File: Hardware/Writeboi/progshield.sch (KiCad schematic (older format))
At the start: 14 parts, among them J1 GB-CART, J2 AUX_POW, SW1 SW_Push, U1 SST39SF040

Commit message: Update capacitor value
Set decoupling capacitor value to 100n
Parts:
- C1: value C -> 100n
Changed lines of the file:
@@
 P 8100 1500
 F 0 "C1" V 7848 1500 50  0000 C CNN
-F 1 "C" V 7939 1500 50  0000 C CNN
+F 1 "100n" V 7939 1500 50  0000 C CNN
 F 2 "Capacitor_THT:CP_Radial_D5.0mm_P2.50mm" H 8138 1350 50  0001 C CNN
 F 3 "~" H 8100 1500 50  0001 C CNN

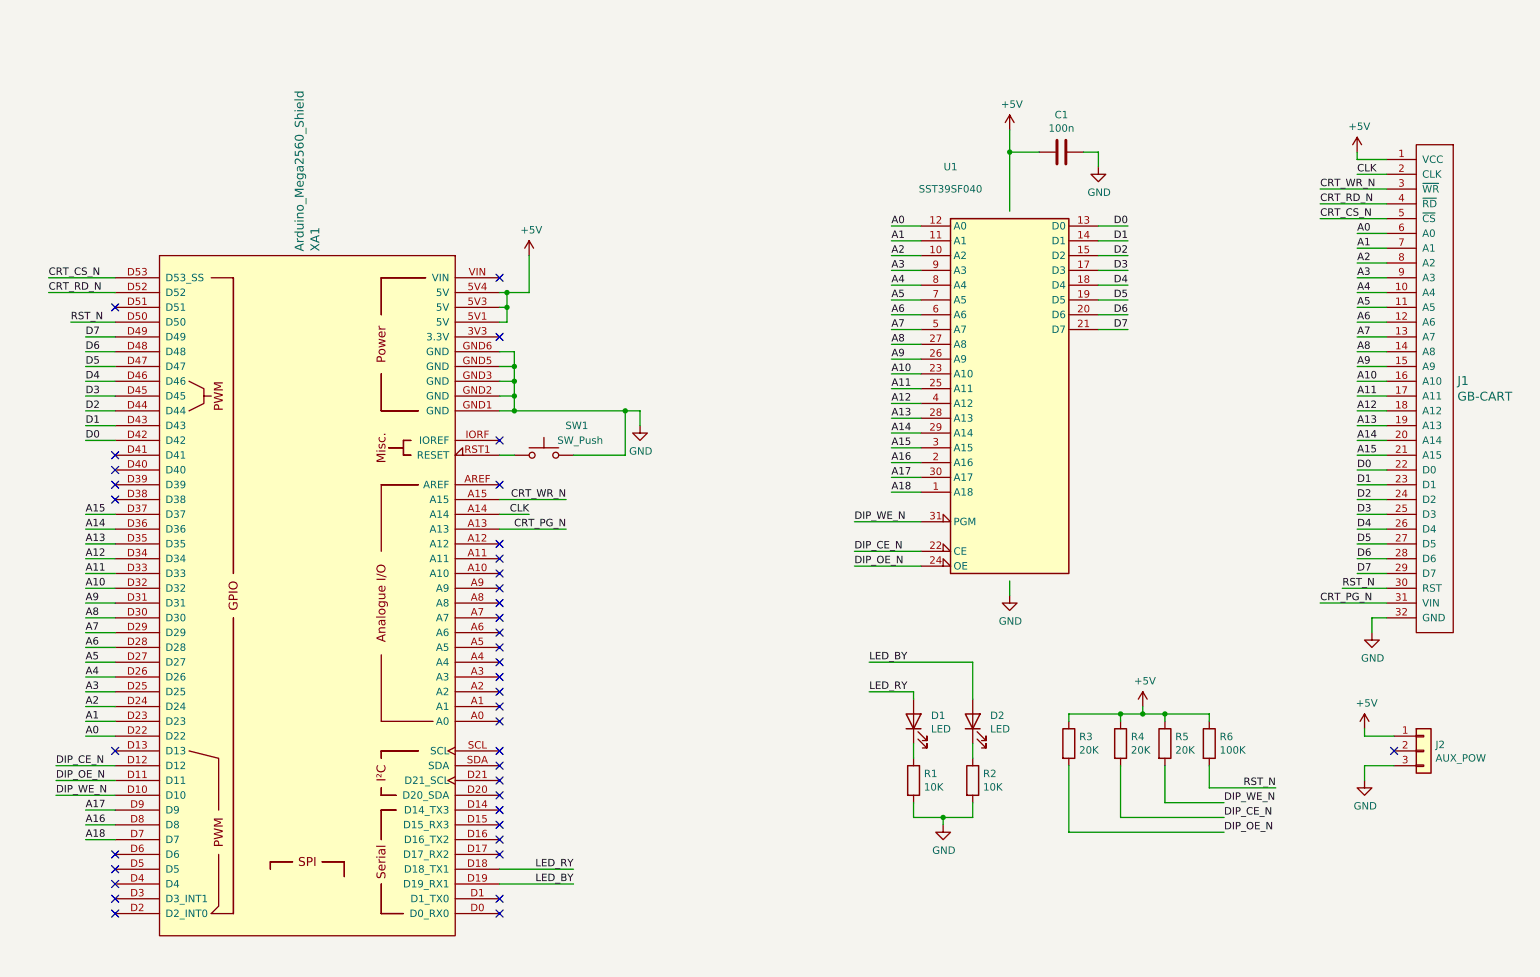
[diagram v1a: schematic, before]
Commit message: Rework schematic
Clean up and reorganize schematic into functional blocks
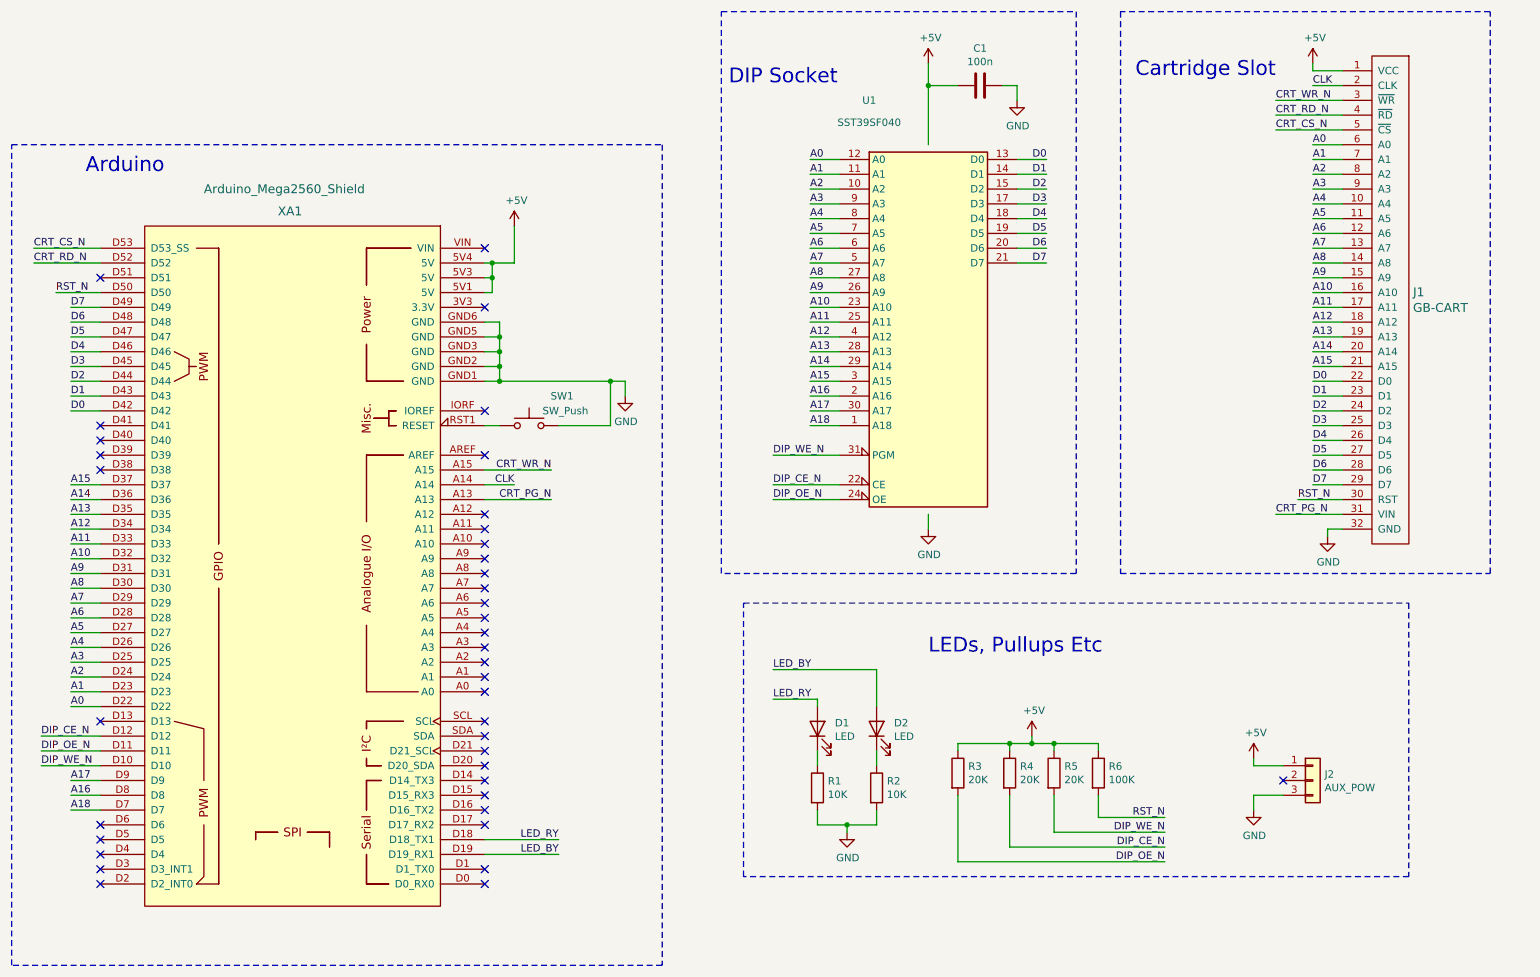
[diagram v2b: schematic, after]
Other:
- note added: "Arduino"
- note added: "Cartridge Slot"
- note added: "DIP Socket"
- note added: "LEDs, Pullups Etc"
- moved on the sheet: C1, D1, D2, J1, J2, R1, R2, R3, R4, R5, R6, SW1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
